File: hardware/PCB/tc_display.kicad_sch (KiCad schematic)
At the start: 29 parts, among them Q1 2N2222, Q2 2N2222, U12 SA15-11SRWA, U13 SA15-11SRWA, U14 SA15-11SRWA, U15 SA15-11SRWA, U16 MAX7219, U17 SA15-11SRWA, U18 SA15-11SRWA, U19 SA15-11SRWA, U20 SA15-11SRWA

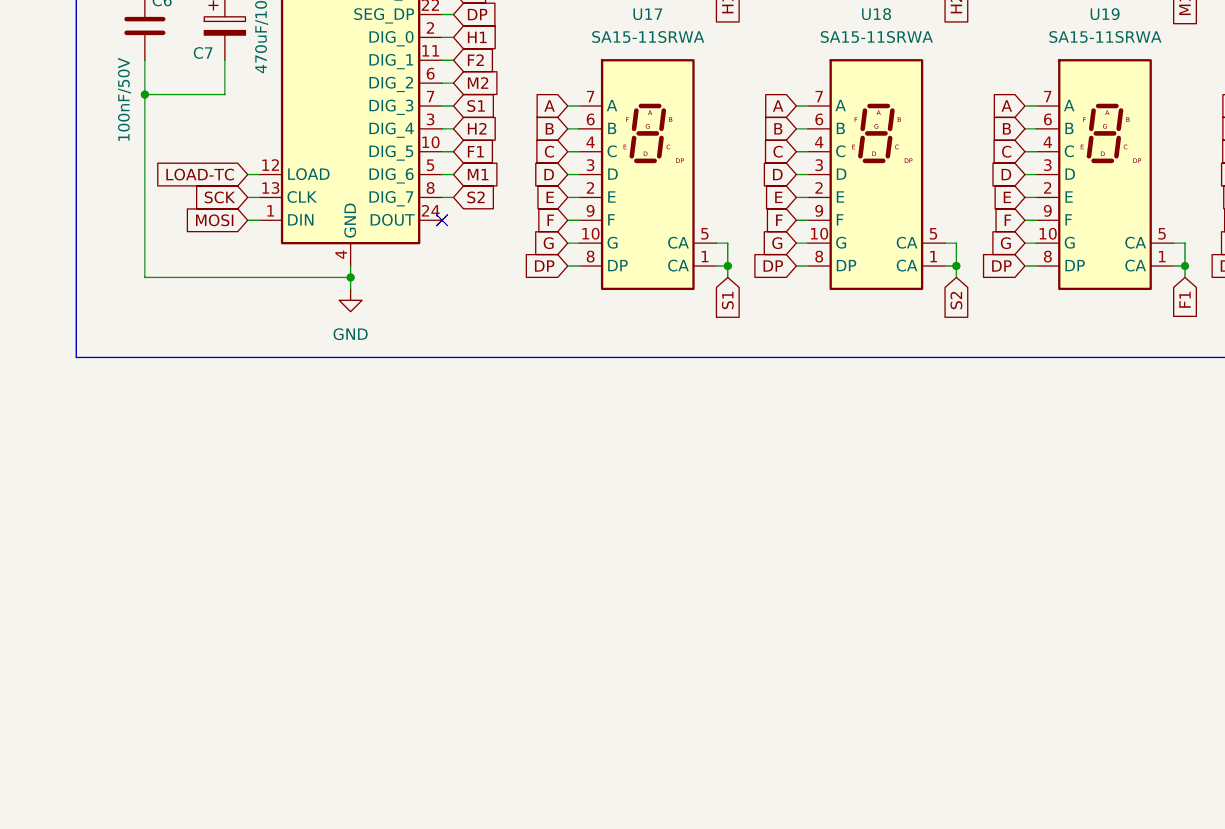
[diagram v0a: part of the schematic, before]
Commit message: KiCAD library MAX7219 added LED driver library updated to access multiple controllers
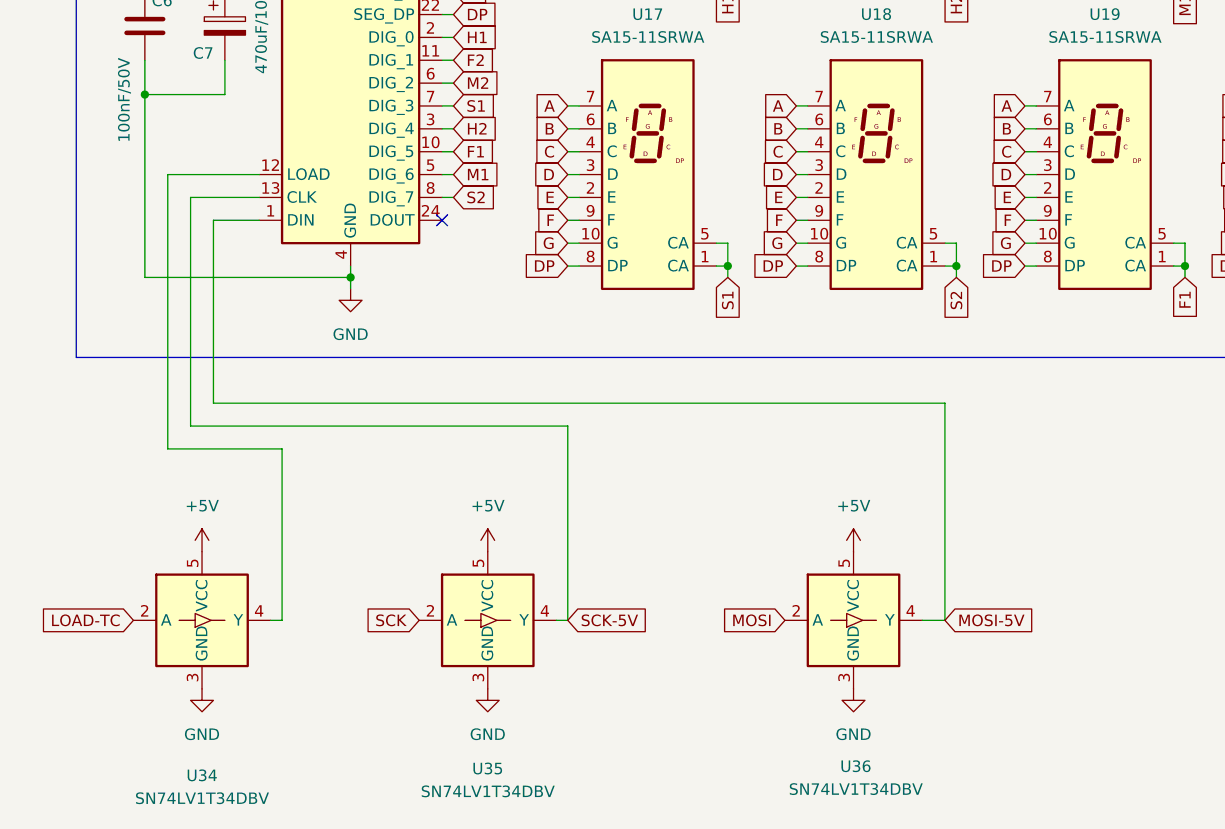
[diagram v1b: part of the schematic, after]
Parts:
- added U34, U35, U36: SN74LV1T34DBV, Package_TO_SOT_SMD:SOT-23-5, symbol Logic_LevelTranslator:SN74LV1T34DBV
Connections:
- net +5V: now also U34.5 (VCC), U35.5 (VCC), U36.5 (VCC)
- net GND: now also U34.3 (GND), U35.3 (GND), U36.3 (GND)
- net LOAD-TC: now also U34.2 (A); no longer U16.12 (LOAD)
- net MOSI: now also U36.2 (A); no longer U16.1 (DIN)
- net SCK: now also U35.2 (A); no longer U16.13 (CLK)
- new net: U16.12 (LOAD), U34.4 (Y)
- new net MOSI-5V: U16.1 (DIN), U36.4 (Y)
- new net SCK-5V: U16.13 (CLK), U35.4 (Y)

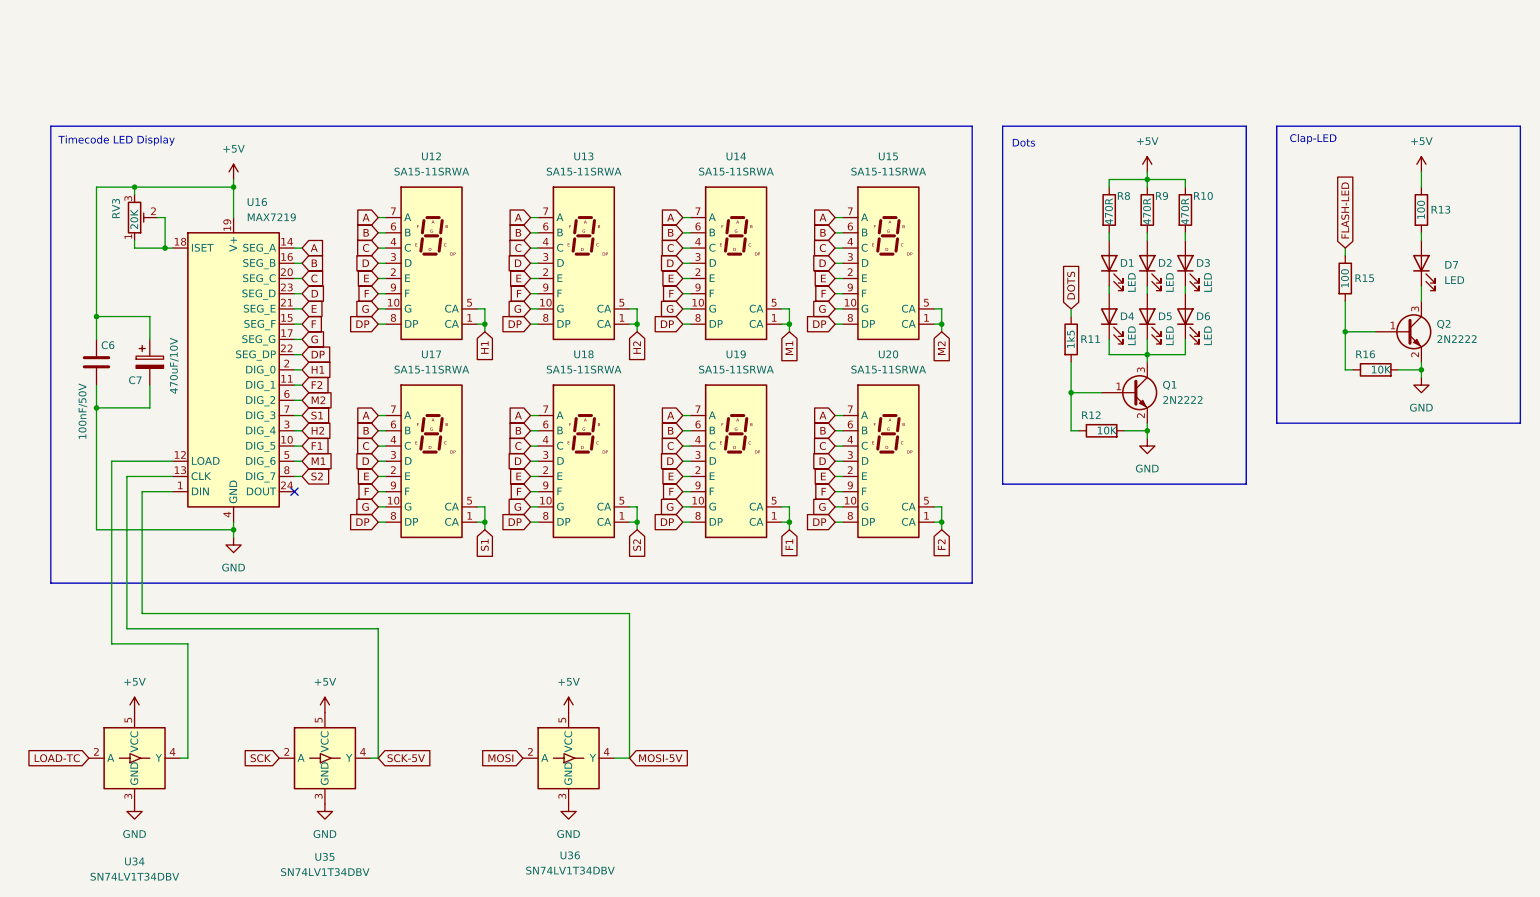
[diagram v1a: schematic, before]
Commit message: capacitors added to signal level converters
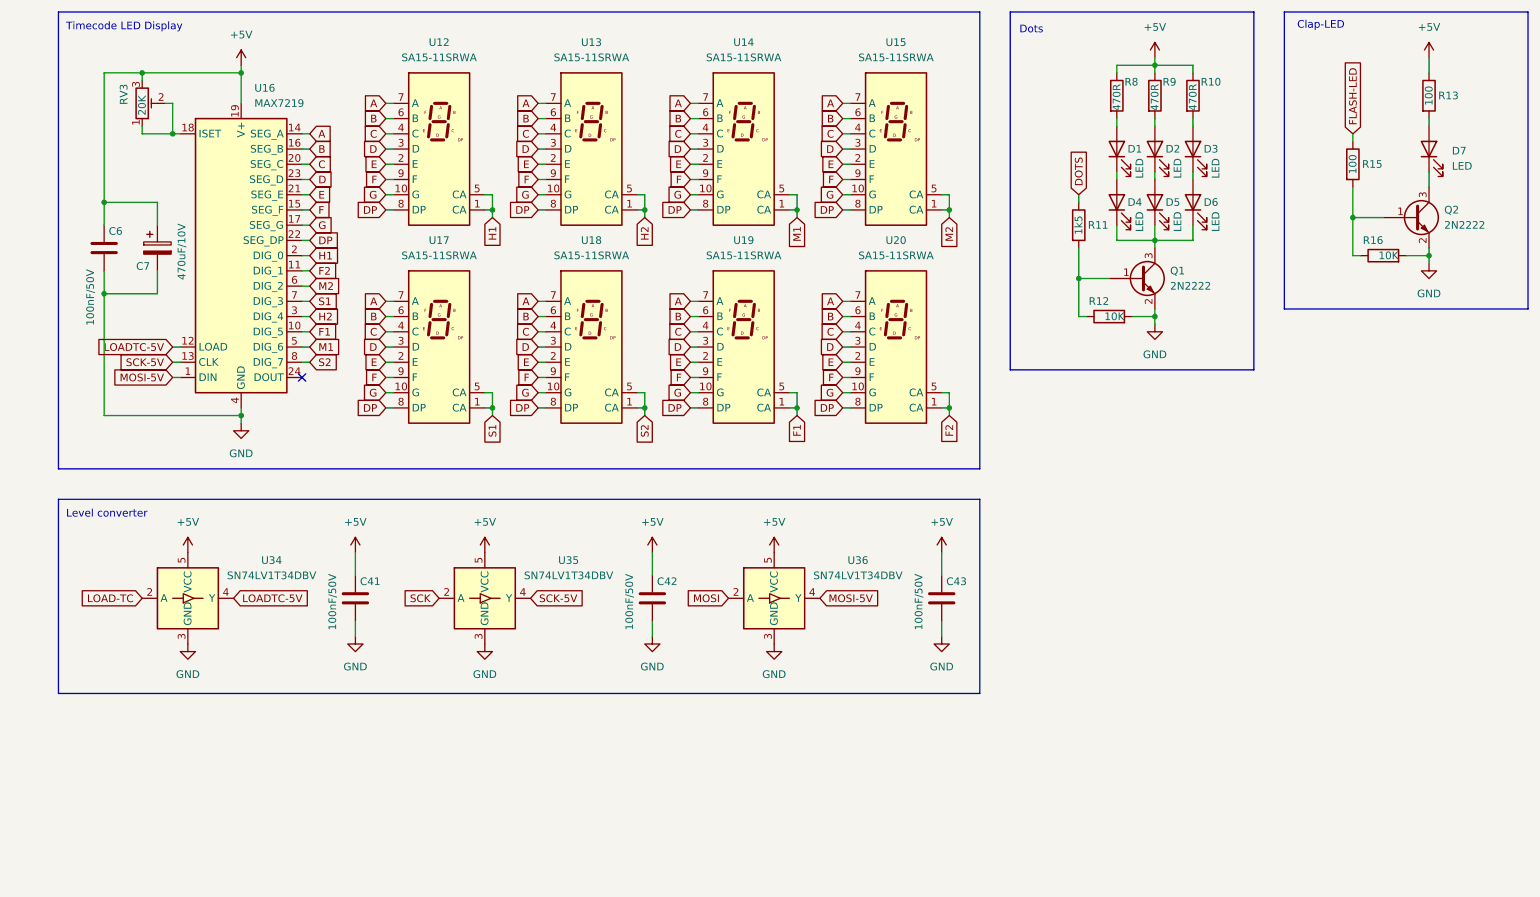
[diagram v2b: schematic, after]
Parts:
- added C41, C42, C43: 100nF/50V, Capacitor_SMD:C_1206_3216Metric_Pad1.33x1.80mm_HandSolder, symbol Device:C
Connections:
- net +5V: now also C41.1, C42.1, C43.1
- net GND: now also C41.2, C42.2, C43.2
- net LOADTC-5V: now reaches U16.12 (LOAD), U34.4 (Y)
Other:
- note added: "Level converter"
- moved on the sheet: C6, C7, D1, D2, D3, D4, D5, D6, D7, Q1, Q2, R10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
